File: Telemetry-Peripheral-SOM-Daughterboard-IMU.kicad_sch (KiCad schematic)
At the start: 6 parts, among them J1 Conn_02x10_Odd_Even, U1 LSM6DSV

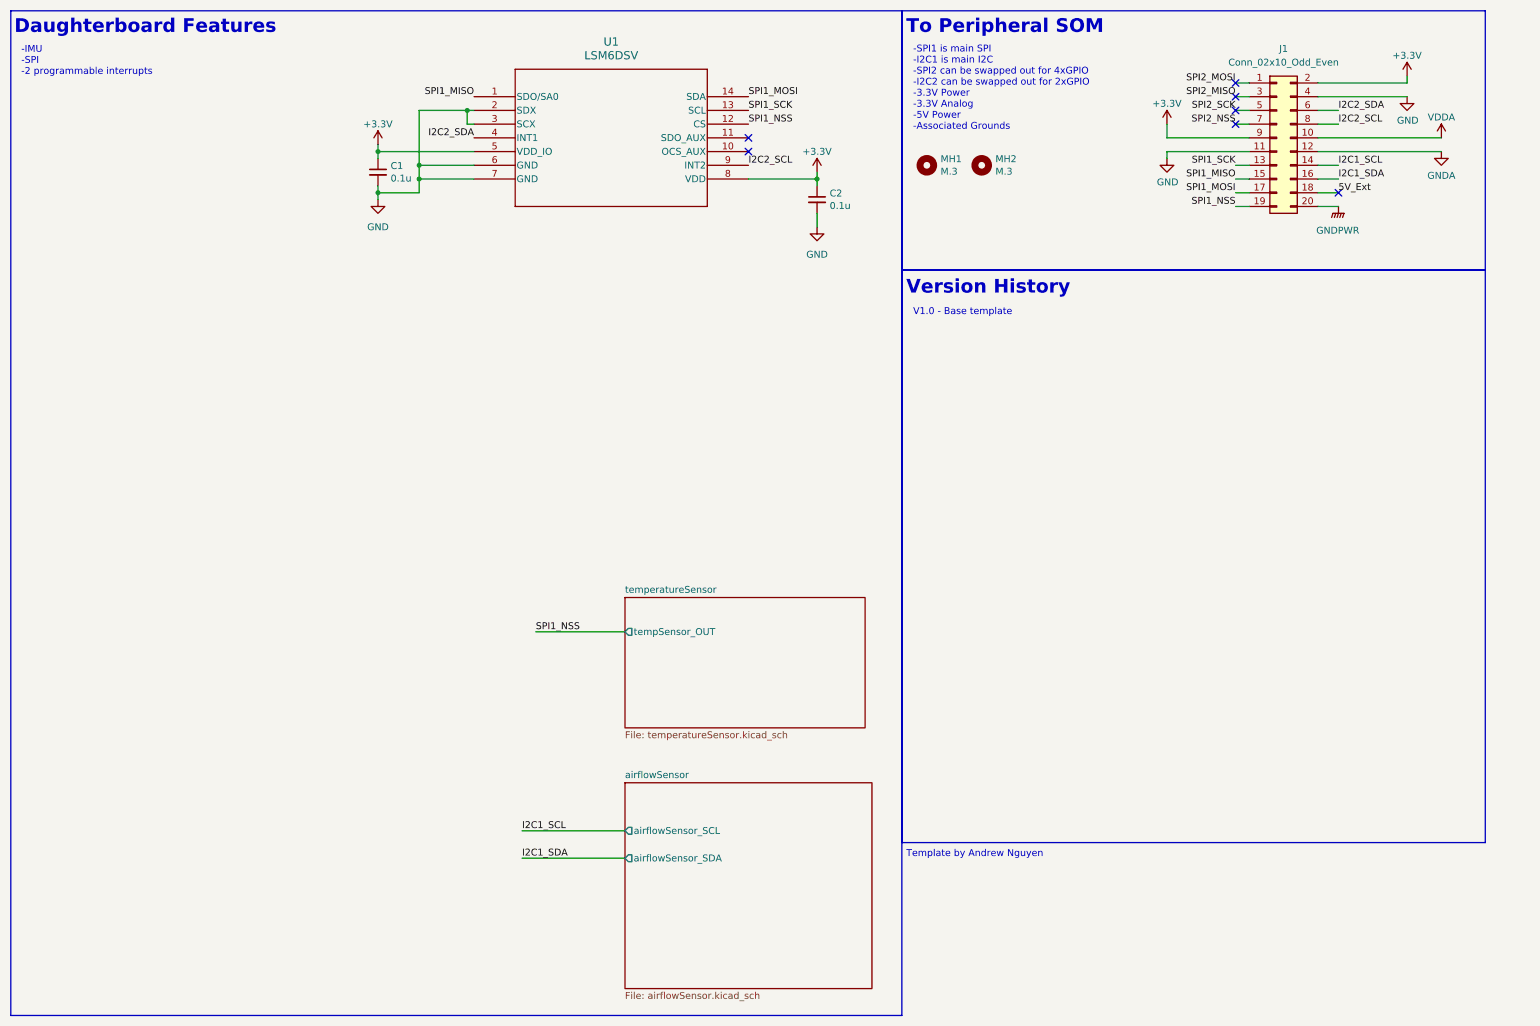
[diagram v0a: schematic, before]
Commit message: made imu sensor into a hierarchical sheet
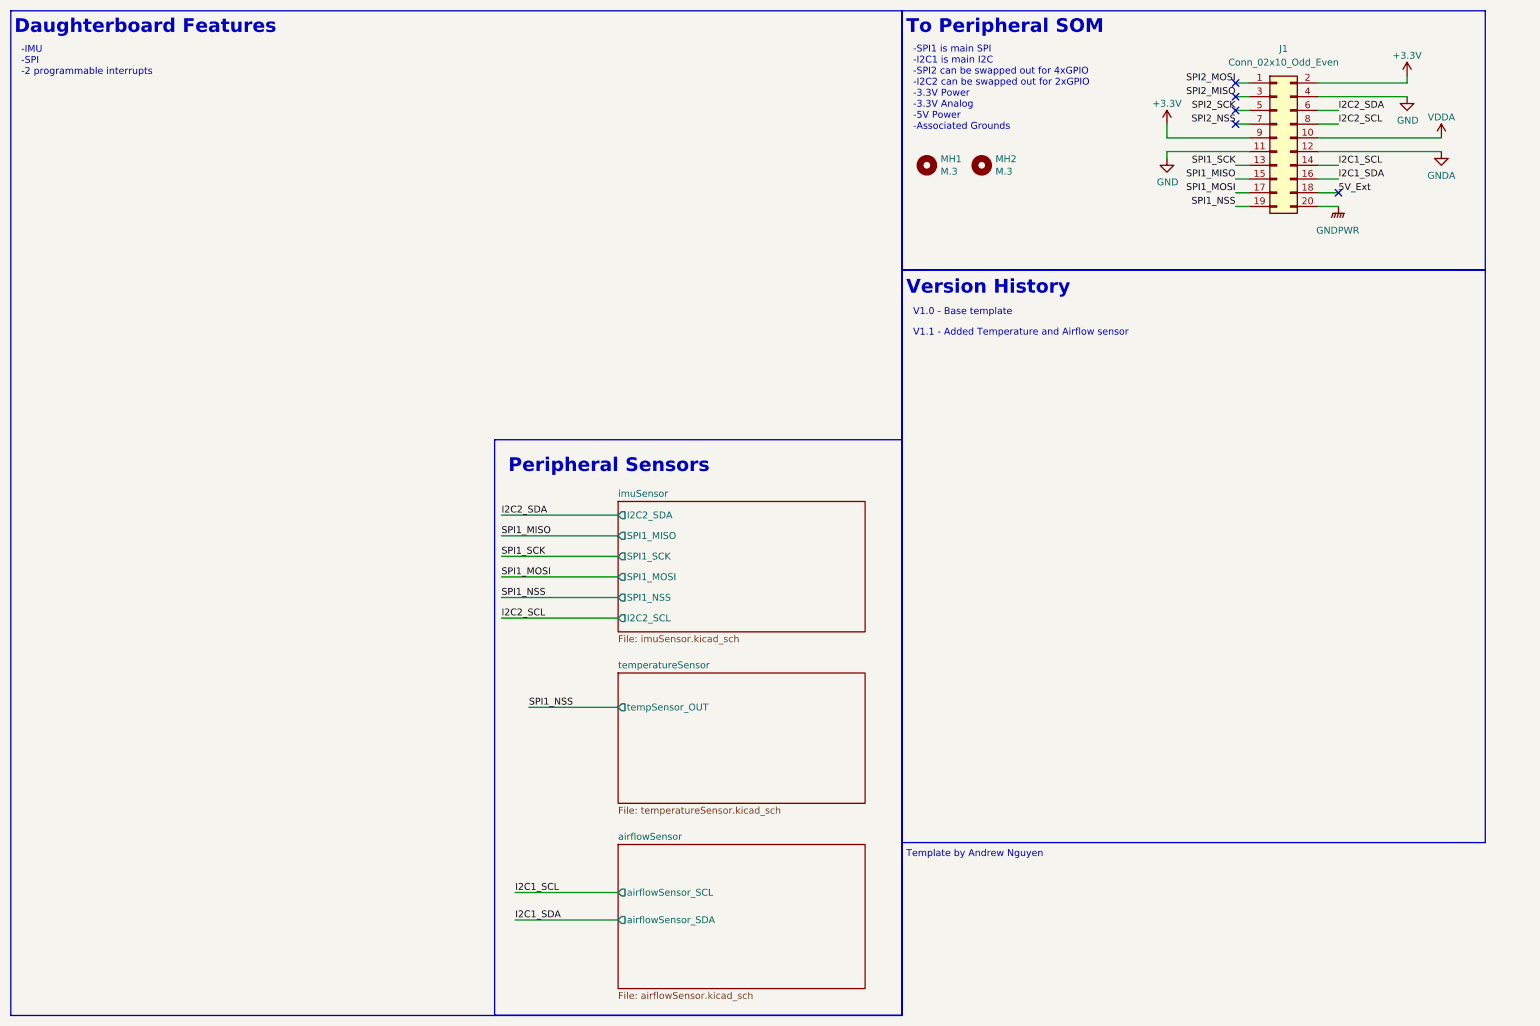
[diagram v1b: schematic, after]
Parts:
- removed C1, C2: 0.1u, Capacitor_SMD:C_0805_2012Metric, symbol Device:C_Small
- removed U1: LSM6DSV, UTSVT_Special:LGA14-L_2P59X3P1X0P5_STM, symbol utsvt-chips:LSM6DSV
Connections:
- no-connect marks 7 -> 5
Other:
- added sheet imuSensor (imuSensor.kicad_sch)
- note added: "Peripheral Sensors"
- note added: "V1.1 - Added Temperature and Airflow sensor"

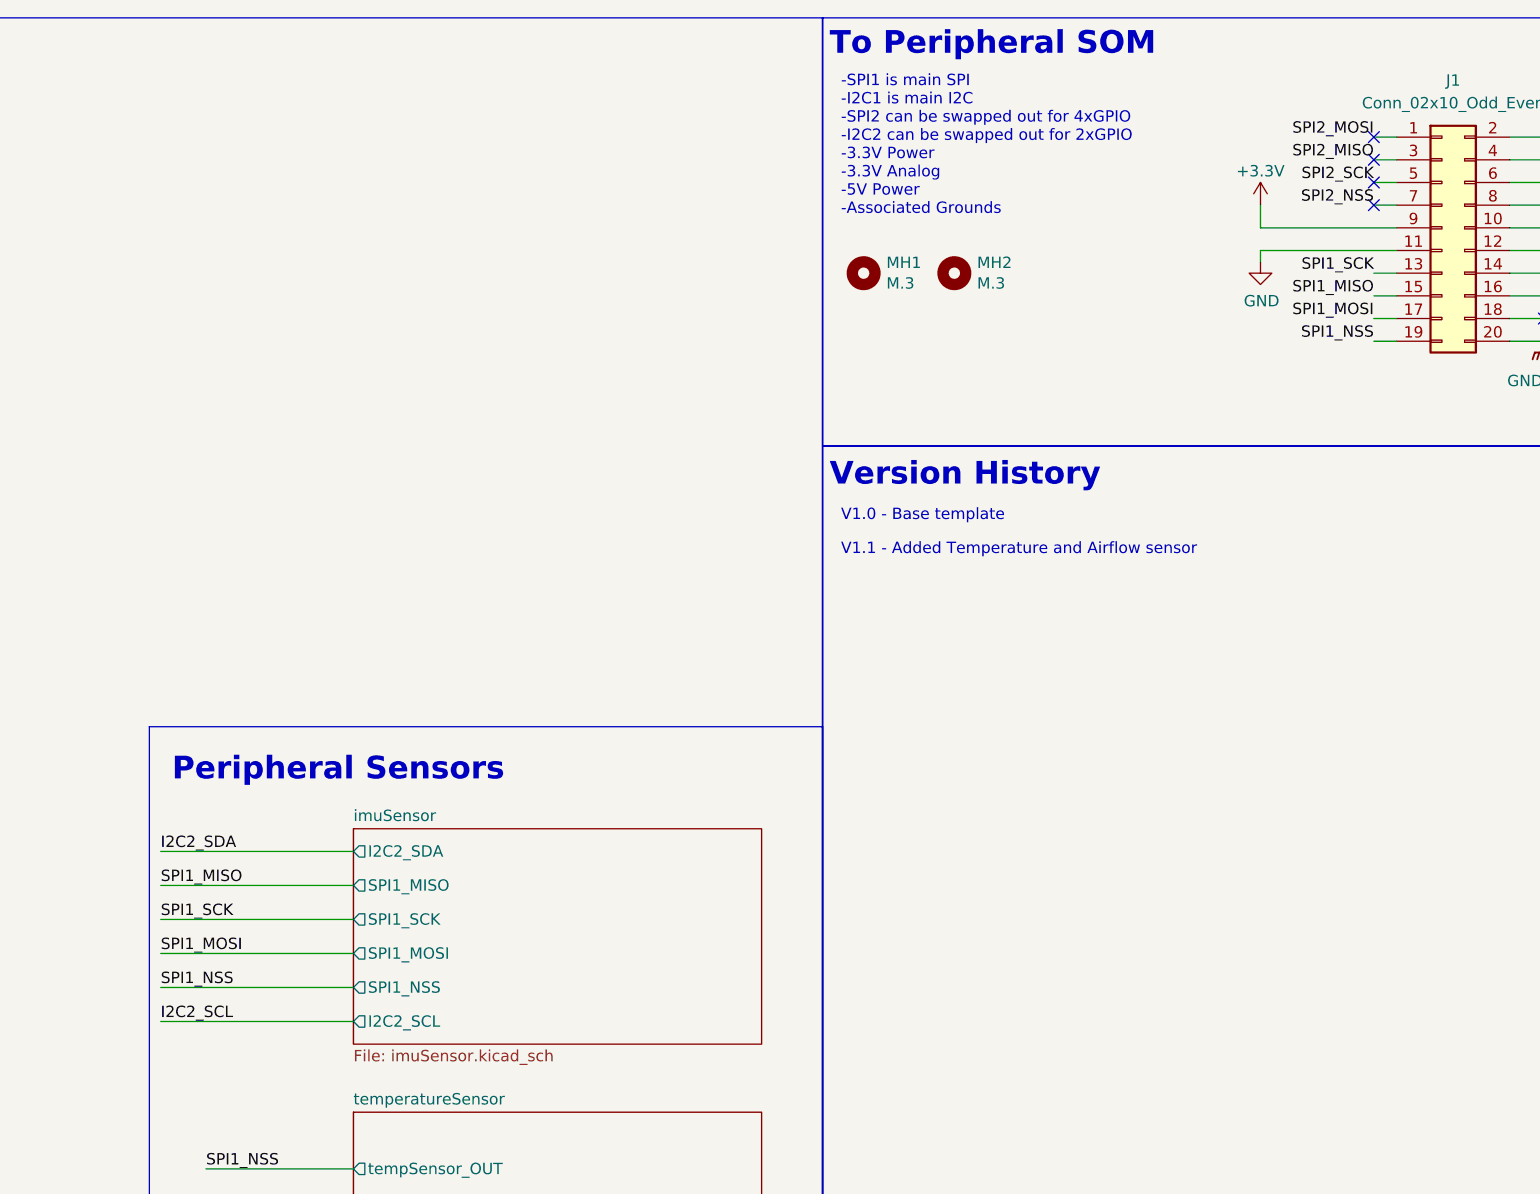
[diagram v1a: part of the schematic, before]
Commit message: fixed spi1_nss conflict, switched imu to spi2
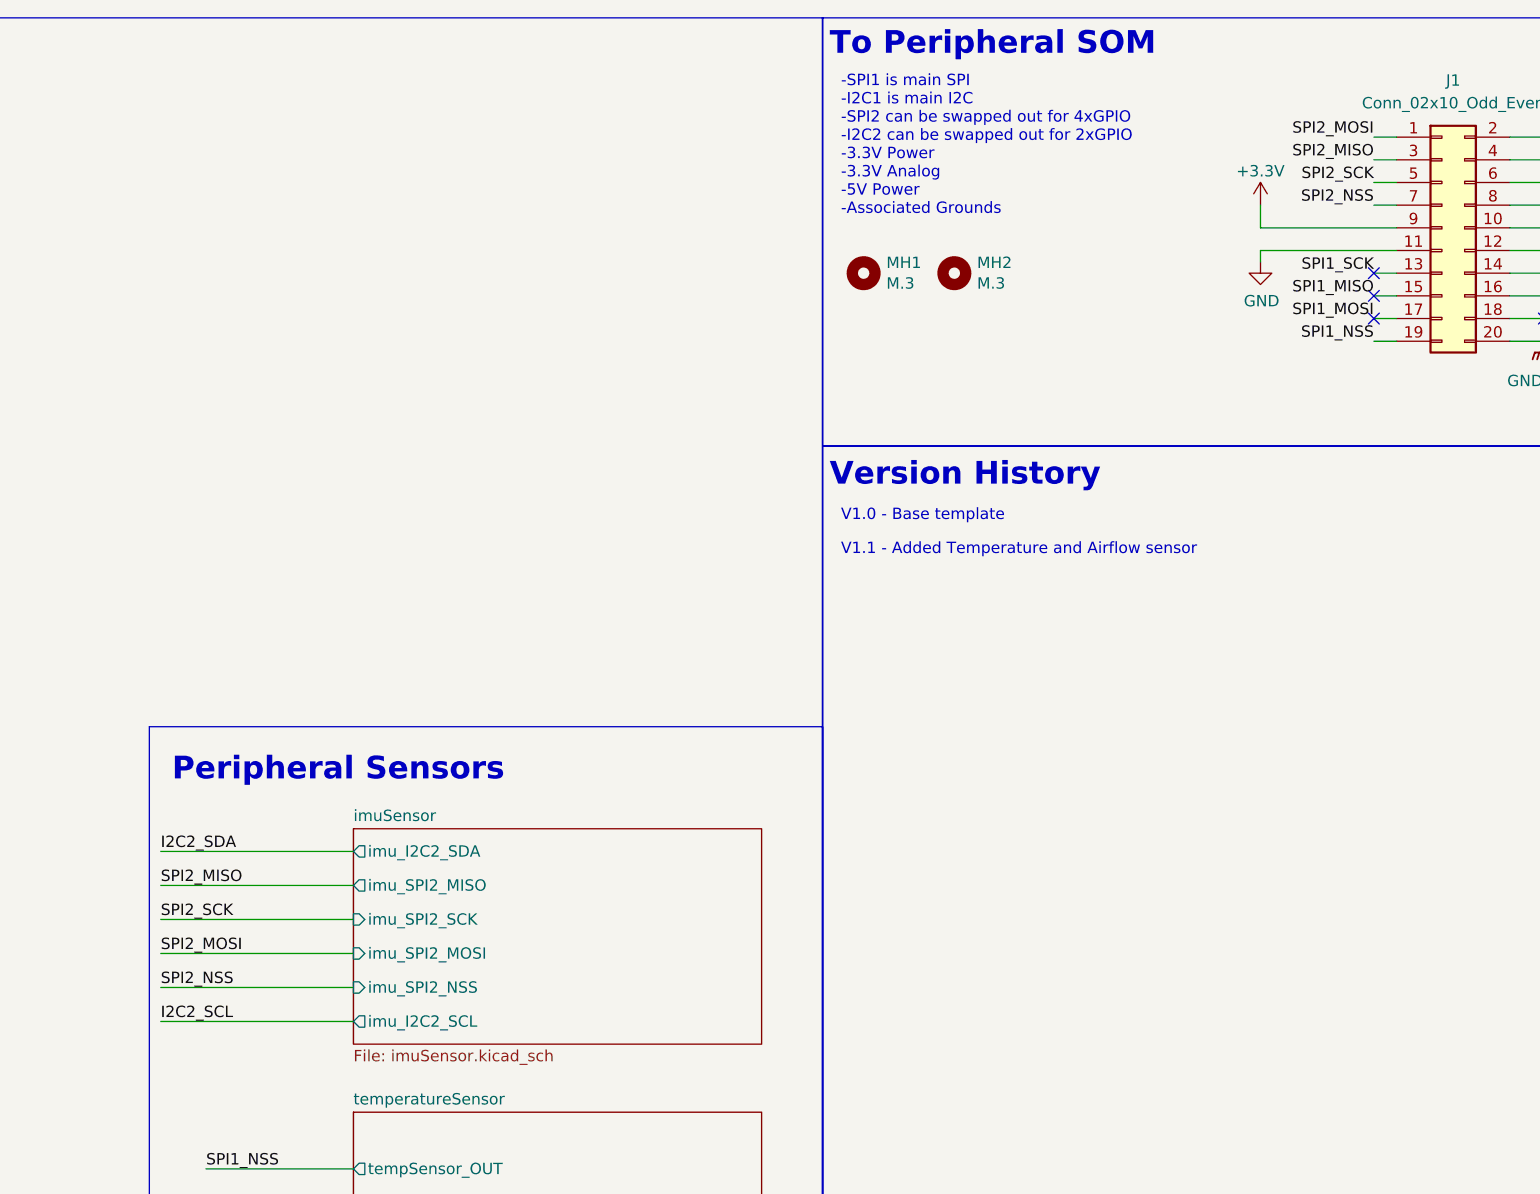
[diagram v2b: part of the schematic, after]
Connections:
- no-connect marks 5 -> 4
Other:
- sheet imuSensor ports: added imu_I2C2_SCL, imu_I2C2_SDA, imu_SPI2_MISO, imu_SPI2_MOSI, imu_SPI2_NSS, imu_SPI2_SCK; removed I2C2_SCL, I2C2_SDA, SPI1_MISO, SPI1_MOSI, SPI1_NSS, SPI1_SCK
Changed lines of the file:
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@@
   (paper "A4")
   (no_connect (at 257.81 45.72))
-  (no_connect (at 238.76 27.94))
-  (no_connect (at 238.76 33.02))
-  (no_connect (at 238.76 25.4))
-  (no_connect (at 238.76 30.48))
+  (no_connect (at 238.76 43.18))
+  (no_connect (at 238.76 40.64))
+  (no_connect (at 238.76 45.72))
   (wire (pts (xy 254 27.94) (xy 270.51 27.94))
     (stroke (width 0) (type default))
@@
     (effects (font (size 2.54 2.54) (thickness 0.508) bold) (justify left bottom))
   )
-  (label "SPI1_NSS" (at 102.87 120.65 0) (fields_autoplaced)
+  (label "SPI2_NSS" (at 102.87 120.65 0) (fields_autoplaced)
     (effects (font (size 1.27 1.27)) (justify left bottom))
   )
@@
     (effects (font (size 1.27 1.27)) (justify left bottom))
   )
-  (label "SPI1_MISO" (at 102.87 109.22 0) (fields_autoplaced)
-    (effects (font (size 1.27 1.27)) (justify left bottom))
-  )
-  (label "SPI1_MOSI" (at 102.87 116.84 0) (fields_autoplaced)
+  (label "SPI2_MISO" (at 102.87 109.22 0) (fields_autoplaced)
+    (effects (font (size 1.27 1.27)) (justify left bottom))
+  )
+  (label "SPI2_MOSI" (at 102.87 116.84 0) (fields_autoplaced)
     (effects (font (size 1.27 1.27)) (justify left bottom))
   )
@@
     (effects (font (size 1.27 1.27)) (justify left bottom))
   )
-  (label "SPI1_SCK" (at 102.87 113.03 0) (fields_autoplaced)
+  (label "SPI2_SCK" (at 102.87 113.03 0) (fields_autoplaced)
     (effects (font (size 1.27 1.27)) (justify left bottom))
   )
@@
       (effects (font (size 1.27 1.27)) (justify left top))
     )
-    (pin "I2C2_SDA" output (at 124.46 105.41 180)
-      (effects (font (size 1.27 1.27)) (justify left))
-    )
-    (pin "SPI1_MISO" output (at 124.46 109.22 180)
-      (effects (font (size 1.27 1.27)) (justify left))
-    )
-    (pin "SPI1_SCK" output (at 124.46 113.03 180)
-      (effects (font (size 1.27 1.27)) (justify left))
-    )
-    (pin "SPI1_MOSI" output (at 124.46 116.84 180)
-      (effects (font (size 1.27 1.27)) (justify left))
-    )
-    (pin "SPI1_NSS" output (at 124.46 120.65 180)
-      (effects (font (size 1.27 1.27)) (justify left))
-    )
-    (pin "I2C2_SCL" output (at 124.46 124.46 180)
-      (effects (font (size 1.27 1.27)) (justify left))
-    )
+    (pin "imu_SPI2_MISO" output (at 124.46 109.22 180)
+      (effects (font (size 1.27 1.27)) (justify left))
+    )
+    (pin "imu_SPI2_MOSI" input (at 124.46 116.84 180)
+      (effects (font (size 1.27 1.27)) (justify left))
+    )
+    (pin "imu_SPI2_SCK" input (at 124.46 113.03 180)
+      (effects (font (size 1.27 1.27)) (justify left))
+    )
+    (pin "imu_I2C2_SCL" output (at 124.46 124.46 180)
+      (effects (font (size 1.27 1.27)) (justify left))
+    )
+    (pin "imu_SPI2_NSS" input (at 124.46 120.65 180)
+      (effects (font (size 1.27 1.27)) (justify left))
+    )
+    (pin "imu_I2C2_SDA" output (at 124.46 105.41 180)
+      (effects (font (size 1.27 1.27)) (justify left))
+    )

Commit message: first draft
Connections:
- net +3.3V: no longer J1.2 (Pin_2)
- net GND: no longer J1.4 (Pin_4)
- new net ADC1_IN: J1.2 (Pin_2)
- new net ADC2_IN: J1.4 (Pin_4)
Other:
- sheet temperatureSensor renamed temperatureSensor1
- added sheet temperatureSensor2 (temperatureSensor2.kicad_sch)
- added sheet temperatureSensor3 (temperatureSensor3.kicad_sch)
- sheet temperatureSensor1 ports: added tempSensor1_OUT; removed tempSensor_OUT
- note added: "V1.2 - Switched imu to utilize spi2 ports"
- note added: "V1.3 - Added all 3 temp sensors' connectors (10/7/23)"
